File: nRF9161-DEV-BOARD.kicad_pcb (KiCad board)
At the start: 4 copper layers, 50 x 34 mm, 84 parts, among them J2 U.FL_LTE_NR+, J20 HOST_1x10_2.54, J5 U.FL_GNSS, J7 nanoSIM_4FF, J8 SWD_10pin, Q1 BSS138, SW2 RESET, U1 NRF9161-LACA-R7, U2 TLV73333PDBV, U3 TPS22919DCKR, U4 TPD3F303DPV, U5 SN74LXC2T45, U6 SN74LXC2T45, U7 SN74LXC1T45, U8 SN74LXC1T45

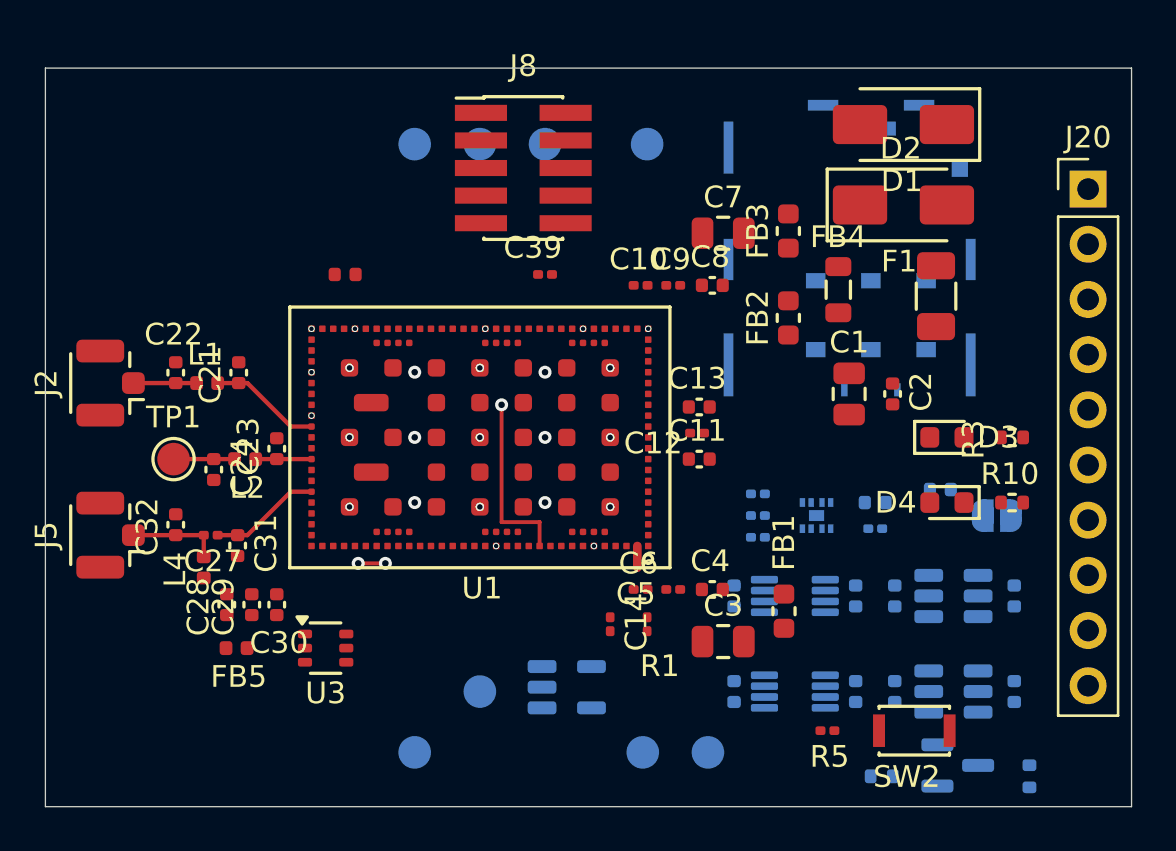
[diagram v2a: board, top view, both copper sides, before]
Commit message: v2 layout 3: bottom re-placed (translators in south strip, SIM ESD under J7), VDD_nRF In2 vias (4 at FB4), RF GND fence vias
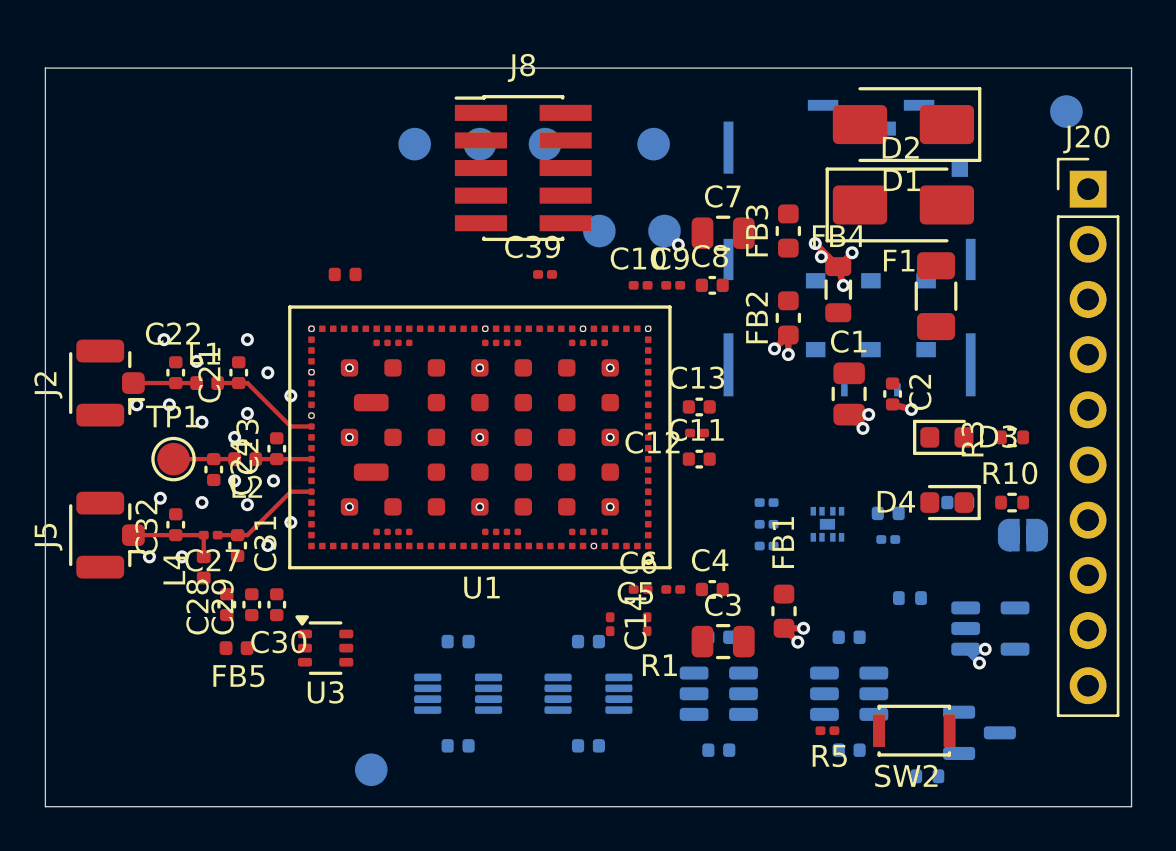
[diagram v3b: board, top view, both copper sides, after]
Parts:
- moved TP17 38.0 mm to (63.0, 17.0)
- moved TP13 24.1 mm to (41.5, 22.5)
- moved TP14 24.1 mm to (44.5, 22.5)
- moved U2 19.7 mm to (59.5, 40.8)
- moved C42 19.6 mm to (35.0, 46.2), turned to 0 degrees
- moved U5 16.1 mm to (35.0, 43.8)
- moved C46 15.3 mm to (47.0, 46.4), turned to 0 degrees
- moved C41 12.9 mm to (35.0, 41.4), turned to 0 degrees
- moved C44 12.6 mm to (41.0, 46.2), turned to 0 degrees
- moved U7 11.7 mm to (47.0, 43.8)
- moved U6 9.50 mm to (41.0, 43.8)
- moved C45 8.32 mm to (47.0, 41.2), turned to 0 degrees
- moved R23 8.30 mm to (55.8, 39.4)
- moved C48 8.07 mm to (53.0, 46.4), turned to 0 degrees
- moved C43 7.08 mm to (41.0, 41.4), turned to 0 degrees
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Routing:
- net VDD_nRF: track 0.00 -> 13.2 mm, vias 0 -> 14
- net COEX0: track 8.25 -> 0.00 mm, vias 1 -> 0
- net SIM_IO: track 1.25 -> 0.00 mm, vias 3 -> 0
- net VDD1: track 1.00 -> 0.00 mm
- net P0.31: vias 1 -> 0
- net GND: vias 22 -> 35

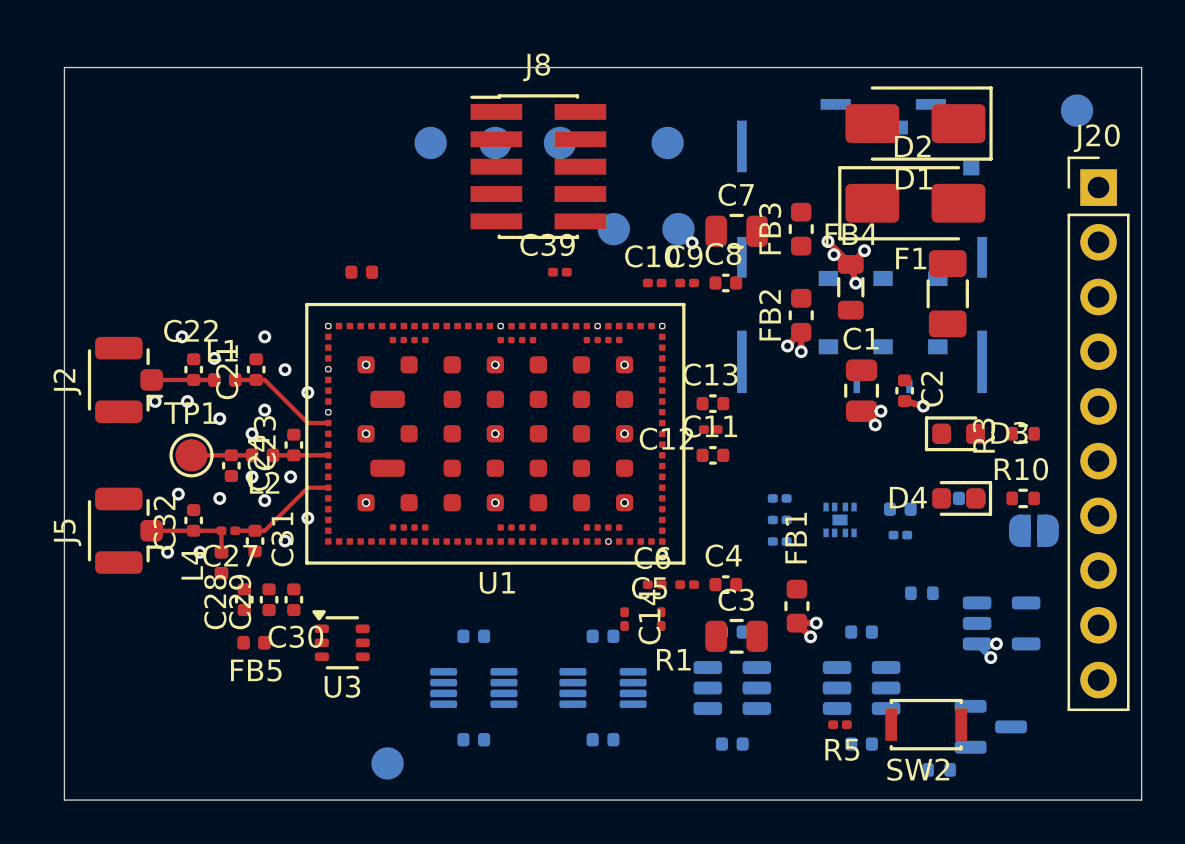
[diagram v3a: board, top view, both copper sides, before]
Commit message: v2 layout 4: all nets routed (Freerouting + scripted A* fixes), SIM ESD block moved below J7, GND islands stitched; unconnected 0, copper DRC 0
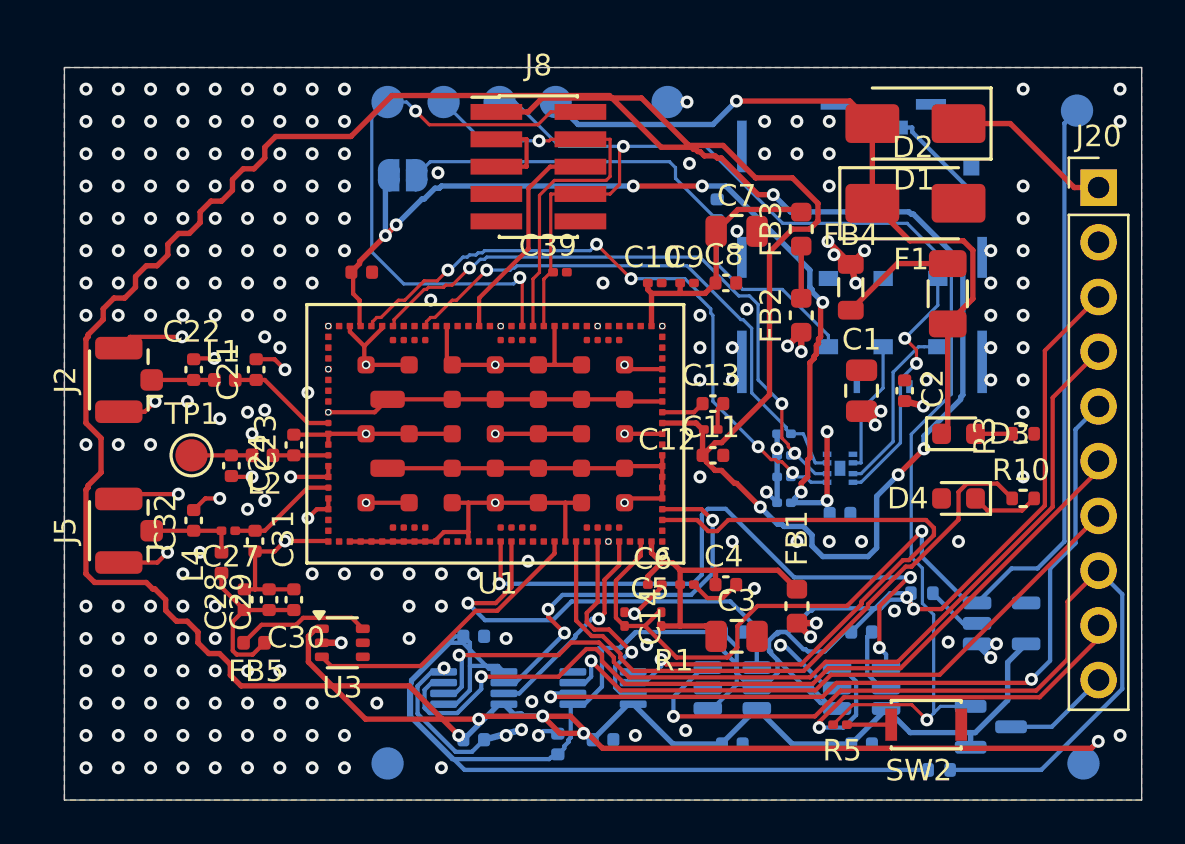
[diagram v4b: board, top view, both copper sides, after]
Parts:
- moved JP2 33.6 mm to (31.7, 20.0)
- moved TP13 33.0 mm to (63.3, 47.3)
- moved C34 17.8 mm to (46.3, 21.6), turned to 90 degrees
- moved TP14 5.92 mm to (44.0, 16.6)
- moved C38 5.60 mm to (49.4, 35.2), turned to 180 degrees
- moved TP15 5.54 mm to (38.8, 16.6)
- moved C43 5.42 mm to (38.9, 46.4), turned to 90 degrees
- moved C36 4.00 mm to (49.4, 32.0), turned to 180 degrees
- moved TP9 3.38 mm to (36.2, 16.6)
- moved TP8 3.06 mm to (33.6, 16.6)
- moved C37 3.01 mm to (49.4, 34.0), turned to 180 degrees
- moved C33 2.81 mm to (52.0, 35.7)
- moved TP7 2.76 mm to (31.0, 16.6)
- moved U4 2.40 mm to (52.0, 33.6), turned to 90 degrees
- moved C35 2.01 mm to (49.4, 33.0), turned to 180 degrees
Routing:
- net VDD_GPIO: track 0.00 -> 220.5 mm, vias 0 -> 9
- net GND: track 0.00 -> 141.0 mm, vias 35 -> 226
- net VIO: track 0.00 -> 119.6 mm, vias 0 -> 2
- net nRESET: track 0.00 -> 64.9 mm, vias 0 -> 2
- net ENABLE: track 0.00 -> 53.1 mm, vias 0 -> 1
- net SIM_1V8: track 0.00 -> 46.8 mm, vias 0 -> 8
- net HOST_DTR: track 0.00 -> 42.7 mm, vias 0 -> 1
- net HOST_TX: track 0.00 -> 42.4 mm, vias 0 -> 1
- net HOST_RTS: track 0.00 -> 40.2 mm, vias 0 -> 1
- net HOST_RX: track 0.00 -> 37.7 mm, vias 0 -> 2
- net VIN: track 0.00 -> 34.4 mm, vias 0 -> 1
- net P0.06: track 0.00 -> 30.8 mm, vias 0 -> 1
- net P0.30: track 0.00 -> 30.4 mm, vias 0 -> 3
- net SIM_IO: track 0.00 -> 30.1 mm, vias 0 -> 5
- net P0.00: track 0.00 -> 29.7 mm
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- added copper zone on B.Cu, net GND
- added copper zone on F.Cu, net GND

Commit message: v2 layout 5: silk refs 1.0/0.15 mm (crowded passives hidden), J20 pin names on silk; silk DRC 0
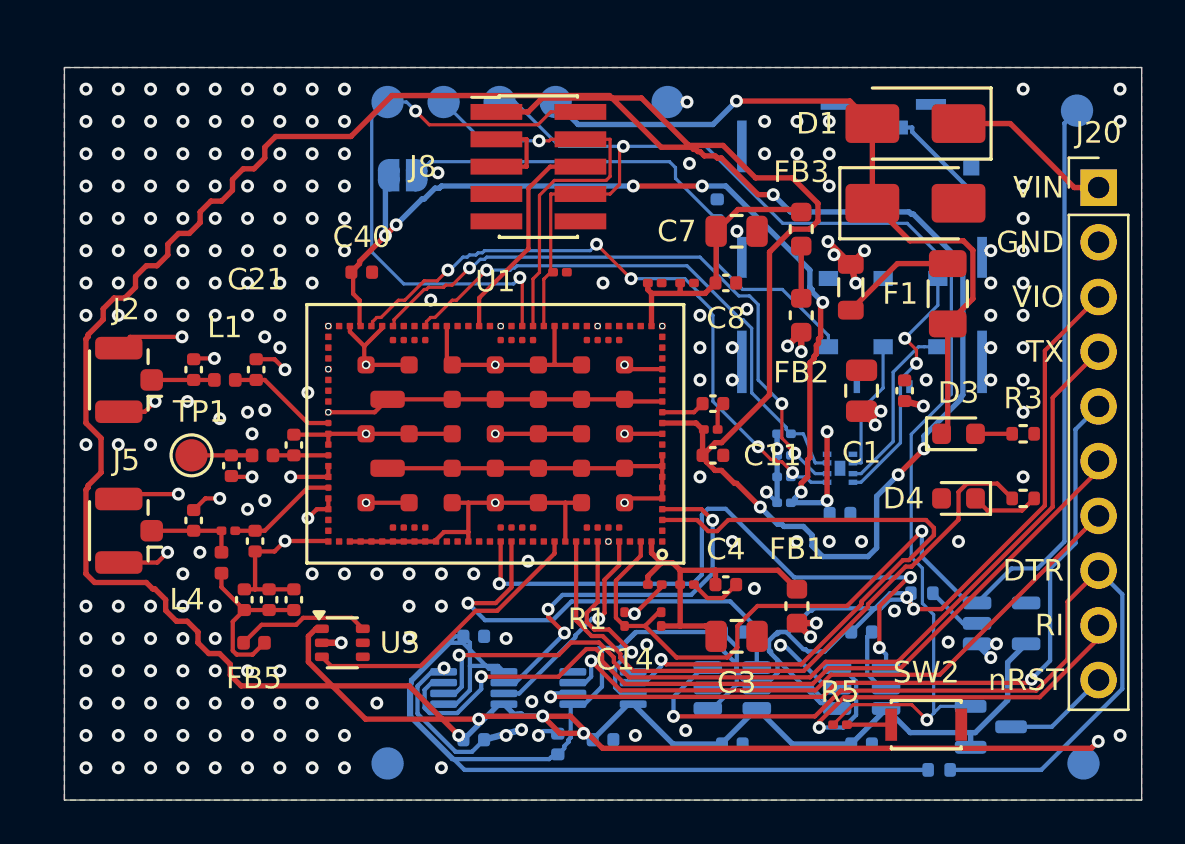
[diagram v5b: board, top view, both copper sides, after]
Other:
- board text added: "CTS"
- board text added: "DTR"
- board text added: "GND"
- board text added: "RI"
- board text added: "RTS"
- board text added: "RX"
- board text added: "TX"
- board text added: "VIN"
- board text added: "VIO"
- board text added: "nRST"

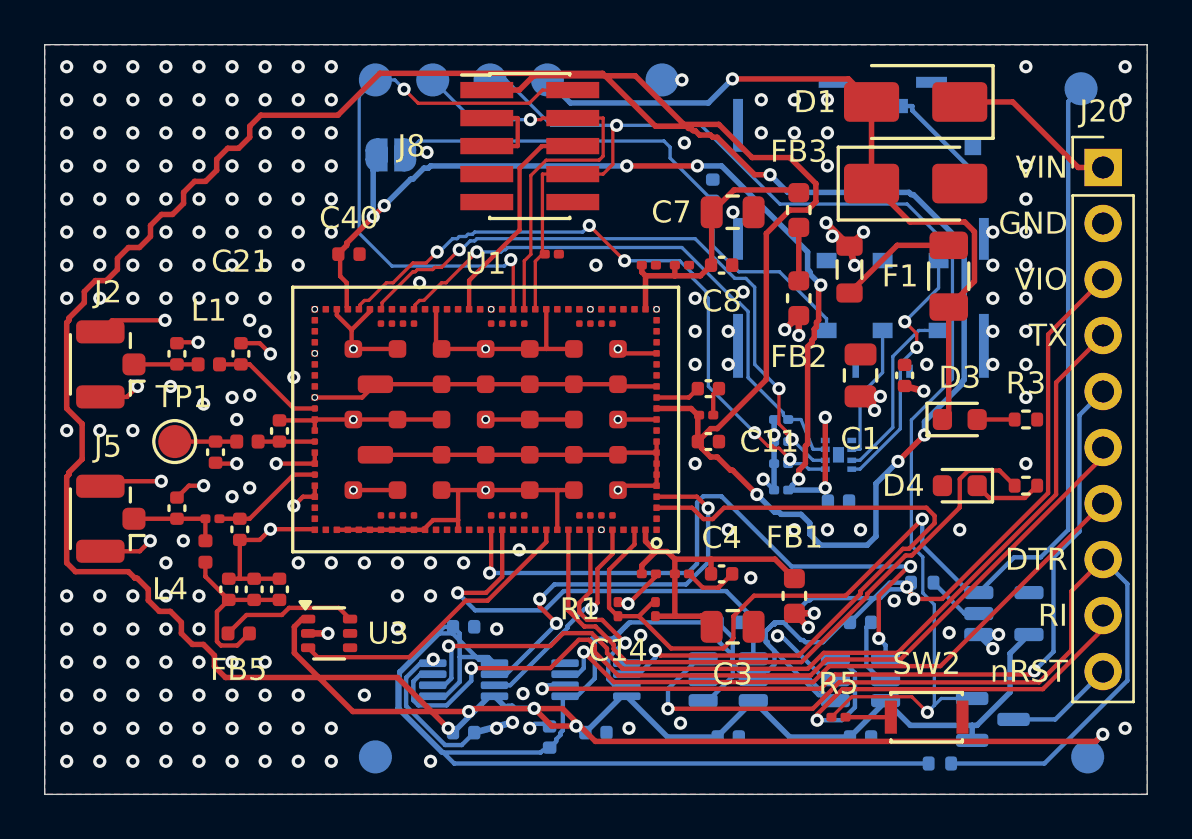
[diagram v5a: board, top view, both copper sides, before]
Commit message: v2 layout 6: VDD_GPIO re-routed outside the RF corner (B5); DRC 0, unconnected 0
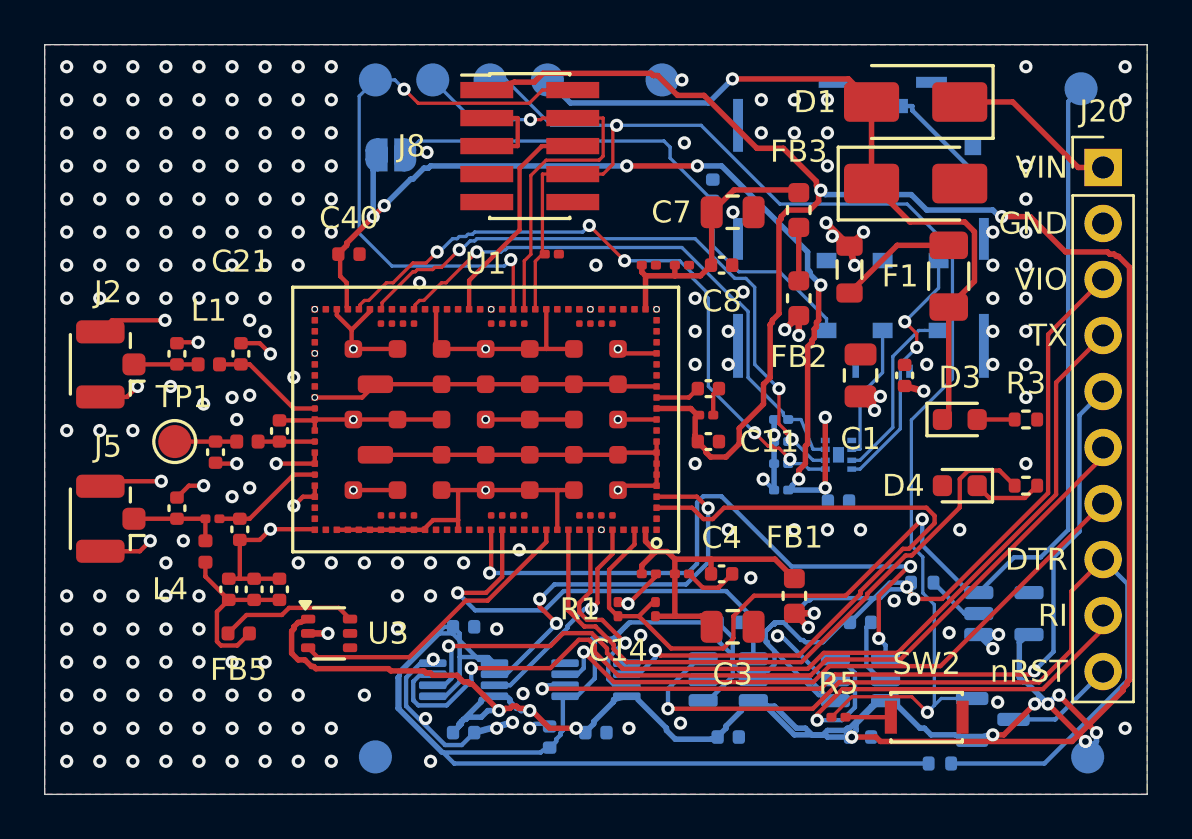
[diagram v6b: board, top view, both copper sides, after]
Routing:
- net VDD_GPIO: track 220.5 -> 147.7 mm, vias 9 -> 12
- net GND: vias 226 -> 228

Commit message: v2b-1: J7 SIM holder moved to TOP (NW corner, board grown 3.5 mm north to 50x37.5), SIM ESD block follows (bottom under J7), SIM nets re-routed; DRC 0, unconnected 0
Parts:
- J7: moved to F.Cu
- moved C33 33.6 mm to (21.5, 21.6)
- moved C35 33.6 mm to (18.9, 18.9)
- moved C36 33.6 mm to (18.9, 17.9)
- moved C37 33.6 mm to (18.9, 19.9)
- moved C38 33.6 mm to (18.9, 21.1)
- moved U4 33.6 mm to (21.5, 19.5)
- moved J7 29.0 mm to (25.8, 19.0), turned to -90 degrees
- moved C34 19.6 mm to (28.2, 14.0), turned to 0 degrees
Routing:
- net SIM_VCC: track 24.7 -> 7.81 mm, vias 0 -> 2
- net SIM_1V8: track 46.8 -> 35.6 mm, vias 8 -> 3
- net GND: track 141.0 -> 151.1 mm, vias 228 -> 177
- net SIM_IO: track 30.1 -> 20.5 mm, vias 5 -> 1
- net SIM_IO_C: track 11.8 -> 3.08 mm, vias 2 -> 1
- net SIM_CLK: track 29.0 -> 22.1 mm, vias 3 -> 1
- net SIM_RST: track 25.7 -> 22.9 mm
- net SIM_CLK_C: track 8.27 -> 6.34 mm, vias 0 -> 1
- net SIM_CD: track 5.69 -> 4.76 mm
- net SIM_RST_C: track 6.19 -> 5.81 mm, vias 0 -> 1
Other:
- board size 50 x 34 mm -> 50 x 37.5 mm
